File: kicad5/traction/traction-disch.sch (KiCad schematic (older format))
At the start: 24 parts

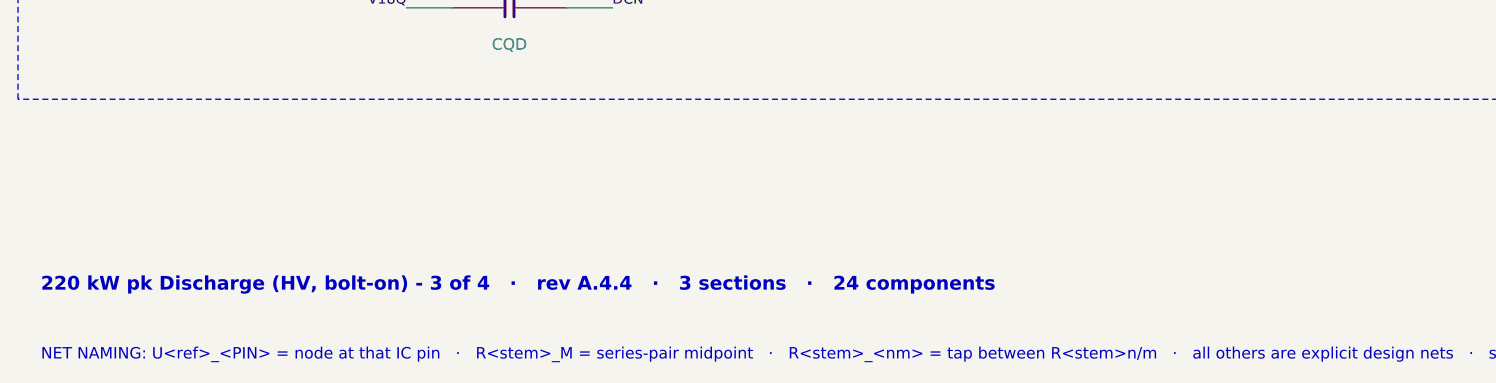
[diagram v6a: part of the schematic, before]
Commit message: Rev A.5: end-to-end documentation refresh + 3 defects the audit caught
Docs (every file rewritten to the released state, history kept as
labeled evidence):
- README: five stacked review paragraphs consolidated into one campaign
  table (F1-F62); new Simulation section with the S1-S7 results table
  and all five SVG plots; badges/stats/mermaids/DFM rows refreshed
  (UCC28C40, four-assembly build flow, 770669-1, sim badge, rev A.5)
- design-basis: gate-drive/LV sections describe the released circuit
  (UCC28C40+BUK7Y14+SMAJ13A clamp, boost->ULDO15 chain, MGJ2+QA01C
  bias set, QA01C +20/-4V note)
- dfm.md + cost-rollup.md rewritten (four assemblies, current tiers,
  76% module share, PO gates, banned-substitute rule)
- EXTRACTED-PARAMS: superseded sections replaced (BUK7Y14, winding
  dots, UCC28C40 UVLO), 10 new part sections, fresh 47-PDF archive
  index with evidence files labeled; SMAJ + TE-770669-1 datasheets
  added; wrong-part PDF from a mirror detected and discarded
- calculations/rev.mjs: single REV source imported by every generator
  (the stale-rev defect class is now structurally impossible)

Defects the audit caught and fixed:
- F60: JVEH was bound to TE 776231-1 "AMPSEAL 23" - its own TE drawing
  shows the 35-pos header (mates 776164). Rebound to 770669-1 (true
  23-pos, mates the 770680-1 plug); drawing archived.
- F61: QA01C DS row is +20/-4V (rails named V18*) - clamps verified
  for +20V; QDIS gate 19.5V vs +22 abs WARN row added.
- F62: the on-sheet ASIL-D + DISCHARGE panel had silently vanished
  from the power sheet as it grew through A.4.x. Placement now retries
  every void and extends the sheet if none fits; a power sheet without
  the panel REFUSES to build. Panel text refreshed (full DRV_EN chain,
  57s bleed, "never energize w/o the DISCHARGE BOARD fitted").

Gates: 1695/1695 pins, ERC 782/0, design-verify 75P/4W/0F, sim-verify
18P/1W/0F, BOM Rs.70,934. Power sheet 44.6x28.6 in (panel row added).

Co-Authored-By: Claude Fable 5 <noreply@ant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
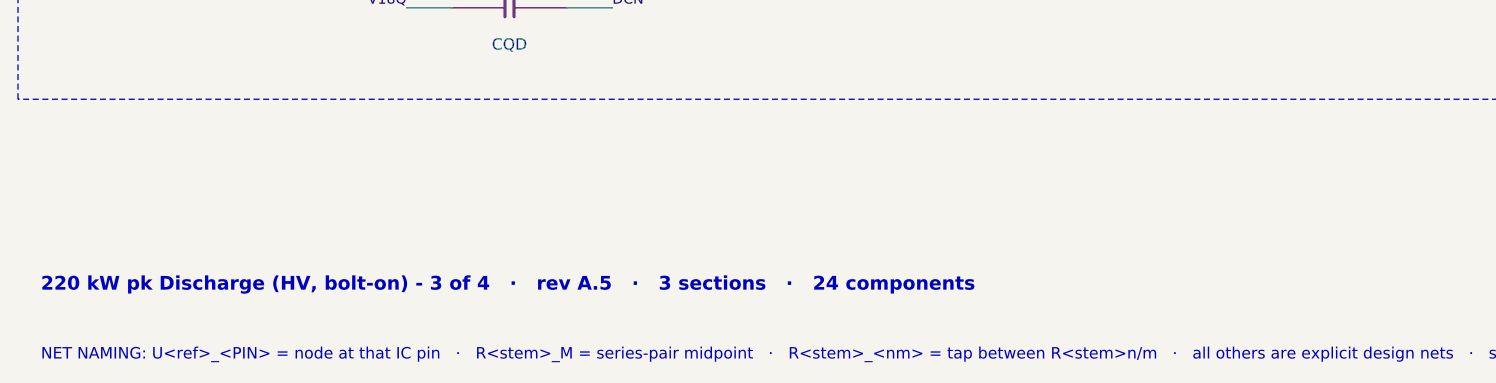
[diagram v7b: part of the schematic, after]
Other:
- note added: "220 kW pk Discharge (HV, bolt-on) - 3 of 4 · rev A.5 · 3 sections · 24 components"
- note removed: "220 kW pk Discharge (HV, bolt-on) - 3 of 4 · rev A.4.4 · 3 sections · 24 components"
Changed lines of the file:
@@
 Title "Traction Inverter — Discharge board (bolt-on, XM3 pattern)"
 Date "2026-09-09"
-Rev "A.4.4"
+Rev "A.5"
 Comp "Traction Inverter 220 kW pk - Discharge (HV, bolt-on), sheet 3 of 4"
 Comment1 "Inverter = Power board + Cap bank busbar + bolt-on Discharge board (all HV) + Control card (LV); safe state holds with any link lost"
@@
 $EndDescr
 Text Notes 600 7100 0    60   ~ 12
-220 kW pk Discharge (HV, bolt-on) - 3 of 4   ·   rev A.4.4   ·   3 sections   ·   24 components
+220 kW pk Discharge (HV, bolt-on) - 3 of 4   ·   rev A.5   ·   3 sections   ·   24 components
 Text Notes 600 7400 0    50   ~ 0
 NET NAMING: U<ref>_<PIN> = node at that IC pin   ·   R<stem>_M = series-pair midpoint   ·   R<stem>_<nm> = tap between R<stem>n/m   ·   all others are explicit design nets   ·   same name on another sheet = same net, joined only at the named connector/stud/tab

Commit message: Rev A.6: review round 6 response, one platform / four SKUs, N7-N9
External review round 6 (46 findings, R-F01..R-F46) was verified finding by
finding and classified in docs/review-A6-disposition.md (+ .csv): 20
Confirmed, 9 Already Fixed, 6 Firmware Handled, 5 Not Applicable,
6 Improvement Recommended. Repo findings F63-F76 are in the verification log.

Hardware (+Rs31/unit, all SKUs unless noted):
- SiC gate 3.3/6.8 ohm; IGBT 1.0/1.0 ohm + 82 pF DESAT blanking (HCG600
  short-circuit rating is 6 us, not 10)
- gate-power flyback start: 2.2 k + 47 uF VDD + 18 V VDD zener (UCC28C40 has
  0.4 V UVLO hysteresis and no clamp); IGBT builds use RT 8.2 k for margin
- fault latch: 10 k / 3.3 nF delay + 15 nF clear one-shot (NSI6611 FLT clears
  only on an EN rising edge, so a fault-dominant latch would deadlock)
- bleeder 2 x 6 x 22 k; HW_ID identity (harness pin 40) and VOFS to the MCU;
  resolver shields to DGND

Platform: one set of PCBs, four SKUs (8XX SiC/IGBT, 4XX IGBT/SiC).
- SKU rows in parts-db, selected by BOM_VARIANT in bom-gen; bom-gen now fails
  on any value/MPN mismatch
- shared calculations/loss-model.mjs
- docs/firmware-contract.md: FW-01..21, safe-state matrix, regen ownership
  (section 4b)
- docs/variants.md: business case

New Road findings:
- N7: LEM HC5FW 900-S/SP1 is a reduced-insulation part, so the phase busbar
  needs a rated sleeve
- N8: TLP152 is UL1577-only; order the (V4) VDE option or an SO6L part
- N9: FW-06 overvoltage response tightened from 100 us to 20 us. With the
  battery path lost at full regen the link reaches 962 V at 100 us and 897 V
  at 20 us; design-verify now checks it

Gates: 602 comps, 1717/1717 pins, ERC 816/0, design-verify 102P/11W/0F,
sim 24P/4W/0F, BOM SiC Rs70,965 / IGBT Rs45,465 @1k.

Co-Authored-By: Claude Opus 5.5 <noreply@anthropic.com>
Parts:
- removed JCTL: HDR-1x4-2.54, HDR1x4, symbol traction-r1:HDR-1x4-2.54
- removed JDCN, JDCP: STUD-M6, StudM6, symbol traction-r1:TERM_1
- added RDIS3, RDIS4: 470R, AxialWW10W, symbol traction-r1:R
- added RQDG: 47R, R0603, symbol traction-r1:R
- added RQDL: 470R, R0603, symbol traction-r1:R
- added RQDPD: 10k, R0603, symbol traction-r1:R
- CQD: renamed from RQDG; value 47R -> 100nF; footprint R0603 -> C0603; symbol traction-r1:R -> traction-r1:C; MPN R0603-47R -> MLCC-100nF-25V
- JCTL: renamed from RBLD1; value 27k -> HDR-1x4-2.54; footprint R2512 -> HDR1x4; symbol traction-r1:R -> traction-r1:HDR-1x4-2.54; MPN R2512-27k-2W -> HDR-1x4-2.54
- JDCN: renamed from RBLD10; value 27k -> STUD-M6; footprint R2512 -> StudM6; symbol traction-r1:R -> traction-r1:TERM_1; MPN R2512-27k-2W -> STUD-M6
- JDCP: renamed from RBLD2; value 27k -> STUD-M6; footprint R2512 -> StudM6; symbol traction-r1:R -> traction-r1:TERM_1; MPN R2512-27k-2W -> STUD-M6
- PSQD: renamed from RDIS2; value 470R -> QA01C-18; footprint AxialWW10W -> SIP7; symbol traction-r1:R -> traction-r1:QA01C-18; MPN WW-470R-10W-AX -> QA01C-18
- QDIS: renamed from RDIS3; value 470R -> HCM75S12T4K3; footprint AxialWW10W -> TO247-4L; symbol traction-r1:R -> traction-r1:HCM75S12T4K3; MPN WW-470R-10W-AX -> HCM75S12T4K3
- RBLD1: renamed from RBLD3; value 27k -> 22k; MPN R2512-27k-2W -> R2512-22k-2W
- RBLD10: renamed from RBLD4; value 27k -> 22k; MPN R2512-27k-2W -> R2512-22k-2W
- RBLD11: renamed from RBLD5; value 27k -> 22k; MPN R2512-27k-2W -> R2512-22k-2W
- RBLD12: renamed from RBLD6; value 27k -> 22k; MPN R2512-27k-2W -> R2512-22k-2W
- RBLD2: renamed from RBLD7; value 27k -> 22k; MPN R2512-27k-2W -> R2512-22k-2W
- RBLD3: renamed from RBLD8; value 27k -> 22k; MPN R2512-27k-2W -> R2512-22k-2W
- RBLD4: renamed from RBLD9; value 27k -> 22k; MPN R2512-27k-2W -> R2512-22k-2W
- RBLD5: renamed from PSQD; value QA01C-18 -> 22k; footprint SIP7 -> R2512; symbol traction-r1:QA01C-18 -> traction-r1:R; MPN QA01C-18 -> R2512-22k-2W
- RBLD6: renamed from QDIS; value HCM75S12T4K3 -> 22k; footprint TO247-4L -> R2512; symbol traction-r1:HCM75S12T4K3 -> traction-r1:R; MPN HCM75S12T4K3 -> R2512-22k-2W
- RBLD7: renamed from UQD; value TLP152 -> 22k; footprint SO6 -> R2512; symbol traction-r1:TLP152 -> traction-r1:R; LCSC C17255258 -> CLASS; MPN TLP152 -> R2512-22k-2W
- RBLD8: renamed from CQD; value 100nF -> 22k; footprint C0603 -> R2512; symbol traction-r1:C -> traction-r1:R; MPN MLCC-100nF-25V -> R2512-22k-2W
- RBLD9: renamed from RDIS1; value 470R -> 22k; footprint AxialWW10W -> R2512; MPN WW-470R-10W-AX -> R2512-22k-2W
- RDIS1: renamed from RQDL; footprint R0603 -> AxialWW10W; MPN R0603-470R -> WW-470R-10W-AX
- RDIS2: renamed from RQDPD; value 10k -> 470R; footprint R0603 -> AxialWW10W; MPN R0603-10k -> WW-470R-10W-AX
- UQD: renamed from RDIS4; value 470R -> TLP152; footprint AxialWW10W -> SO6; symbol traction-r1:R -> traction-r1:TLP152; LCSC CLASS -> C17255258; MPN WW-470R-10W-AX -> TLP152
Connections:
- net labels added: BL05, BL15
- wire segments 55 -> 59
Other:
- note added: "220 kW pk Discharge (HV, bolt-on) - 3 of 4 · rev A.6 · 3 sections · 26 components"
- note removed: "220 kW pk Discharge (HV, bolt-on) - 3 of 4 · rev A.5 · 3 sections · 24 components"
- moved on the sheet: RBLD1, RBLD10, RBLD11, RBLD12, RBLD2, RBLD3, RBLD4, RBLD9, RDIS1, RDIS2
